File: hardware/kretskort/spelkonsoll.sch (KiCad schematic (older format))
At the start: 2 parts, among them U2 ESP32-DEVKITC-32D, U3 ILI9488

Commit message: more circuit board kicad files
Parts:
- added BZ1: Buzzer, Buzzer_Beeper:Buzzer_15x7.5RM7.6, symbol Device:Buzzer
- added SW1, SW10, SW2, SW3, SW4, SW5, SW6, SW7, SW8, SW9: SW_Push, Button_Switch_THT:SW_TH_Tactile_Omron_B3F-10xx, symbol Switch:SW_Push
- added SW11, SW12: SW_Push, Button_Switch_THT:SW_Tactile_SPST_Angled_PTS645Vx83-2LFS, symbol Switch:SW_Push
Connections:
- net +5V: now also SW1.2, SW10.2, SW11.2, SW12.2, SW2.2, SW3.2, SW4.2, SW5.2, SW6.2, SW7.2, SW8.2, SW9.2
- net GND: now also BZ1.2 (+); no longer U2.18 (CMD)
- net BTN_SELECT: now reaches U2.10 (IO26)
- net BTN_SELECT: now also SW10.1
- net BTN_DP_UP: now reaches U2.11 (IO27)
- net BTN_DP_UP: now also SW5.1
- net BTN_DP_DOWN: now reaches U2.12 (IO14)
- net BTN_DP_DOWN: now also SW6.1
- net BTN_DP_LEFT: now reaches U2.13 (IO12)
- net BTN_DP_LEFT: now also SW7.1
- net BTN_DP_RIGHT: now reaches U2.15 (IO13)
- net BTN_DP_RIGHT: now also SW8.1
- net BUZZER: now reaches U2.25 (IO21)
- net BUZZER: now also BZ1.1 (-)
- net BTN_BUMPER_L: now reaches U2.30 (IO17)
- net BTN_BUMPER_L: now also SW11.1
- net BTN_BUMPER_R: now reaches U2.31 (IO16)
- net BTN_BUMPER_R: now also SW12.1
- net BTN_A: now reaches U2.5 (IO34)
- net BTN_A: now also SW1.1
- net BTN_B: now reaches U2.6 (IO35)
- net BTN_B: now also SW2.1
- net BTN_X: now reaches U2.7 (IO32)
- net BTN_X: now also SW3.1
- net BTN_Y: now reaches U2.8 (IO33)
- net BTN_Y: now also SW4.1
- net BTN_START: now reaches U2.9 (IO25)
- net BTN_START: now also SW9.1
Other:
- note added: "BUTTONS 'N BUMPERS"
- note added: "BUZZER"
- moved on the sheet: U2, U3

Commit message: modified pcb to fit new design
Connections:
- net +5V: no longer SW1.2, SW10.2, SW11.2, SW12.2, SW2.2, SW3.2, SW4.2, SW5.2, SW6.2, SW7.2, SW8.2, SW9.2
- net GND: now also SW1.2, SW10.2, SW11.2, SW12.2, SW2.2, SW3.2, SW4.2, SW5.2, SW6.2, SW7.2, SW8.2, SW9.2
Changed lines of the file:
@@
 	1    0    0    -1
-$EndComp
-$Comp
-L power:+5V #PWR0104
-U 1 1 6203BB27
-P 9300 5100
-F 0 "#PWR0104" H 9300 4950 50  0001 C CNN
-F 1 "+5V" V 9315 5228 50  0000 L CNN
-F 2 "" H 9300 5100 50  0001 C CNN
-F 3 "" H 9300 5100 50  0001 C CNN
-	1    9300 5100
-	0    1    1    0
 $EndComp
 Wire Wire Line
@@
 Text GLabel 2850 3650 0    50   Input ~ 0
 BTN_A
-$Comp
-L power:+5V #PWR0108
-U 1 1 6203E5CA
-P 9300 5500
-F 0 "#PWR0108" H 9300 5350 50  0001 C CNN
-F 1 "+5V" V 9315 5628 50  0000 L CNN
-F 2 "" H 9300 5500 50  0001 C CNN
-F 3 "" H 9300 5500 50  0001 C CNN
-	1    9300 5500
-	0    1    1    0
-$EndComp
 Wire Wire Line
 	9200 5500 9300 5500
@@
 Text GLabel 8800 6300 0    50   Input ~ 0
 BTN_Y
-$Comp
-L power:+5V #PWR01
-U 1 1 6204640C
-P 9300 5900
-F 0 "#PWR01" H 9300 5750 50  0001 C CNN
-F 1 "+5V" V 9315 6028 50  0000 L CNN
-F 2 "" H 9300 5900 50  0001 C CNN
-F 3 "" H 9300 5900 50  0001 C CNN
-	1    9300 5900
-	0    1    1    0
-$EndComp
-$Comp
-L power:+5V #PWR02
-U 1 1 620466A0
-P 9300 6300
-F 0 "#PWR02" H 9300 6150 50  0001 C CNN
-F 1 "+5V" V 9315 6428 50  0000 L CNN
-F 2 "" H 9300 6300 50  0001 C CNN
-F 3 "" H 9300 6300 50  0001 C CNN
-	1    9300 6300
-	0    1    1    0
-$EndComp
 Wire Wire Line
 	9300 6300 9200 6300
@@
 	1    0    0    -1
 $EndComp
-$Comp
-L power:+5V #PWR0109
-U 1 1 6205AD69
-P 10800 5100
-F 0 "#PWR0109" H 10800 4950 50  0001 C CNN
-F 1 "+5V" V 10815 5228 50  0000 L CNN
-F 2 "" H 10800 5100 50  0001 C CNN
-F 3 "" H 10800 5100 50  0001 C CNN
-	1    10800 5100
-	0    1    1    0
-$EndComp
 Wire Wire Line
 	10800 5100 10700 5100
@@
 Text GLabel 10300 5500 0    50   Input ~ 0
 BTN_SELECT
-$Comp
-L power:+5V #PWR0110
-U 1 1 6205FBF8
-P 10800 5500
-F 0 "#PWR0110" H 10800 5350 50  0001 C CNN
-F 1 "+5V" V 10815 5628 50  0000 L CNN
-F 2 "" H 10800 5500 50  0001 C CNN
-F 3 "" H 10800 5500 50  0001 C CNN
-	1    10800 5500
-	0    1    1    0
-$EndComp
 Wire Wire Line
 	10800 5500 10700 5500
@@
 	1    7800 6300
 	1    0    0    -1
-$EndComp
-$Comp
-L power:+5V #PWR0111
-U 1 1 620917FA
-P 8100 5100
-F 0 "#PWR0111" H 8100 4950 50  0001 C CNN
-F 1 "+5V" V 8115 5228 50  0000 L CNN
-F 2 "" H 8100 5100 50  0001 C CNN
-F 3 "" H 8100 5100 50  0001 C CNN
-	1    8100 5100
-	0    1    1    0
-$EndComp
-$Comp
-L power:+5V #PWR0112
-U 1 1 62092742
-P 8100 5500
-F 0 "#PWR0112" H 8100 5350 50  0001 C CNN
-F 1 "+5V" V 8115 5628 50  0000 L CNN
-F 2 "" H 8100 5500 50  0001 C CNN
-F 3 "" H 8100 5500 50  0001 C CNN
-	1    8100 5500
-	0    1    1    0
-$EndComp
-$Comp
-L power:+5V #PWR0113
-U 1 1 62092987
-P 8100 5900
-F 0 "#PWR0113" H 8100 5750 50  0001 C CNN
-F 1 "+5V" V 8115 6028 50  0000 L CNN
-F 2 "" H 8100 5900 50  0001 C CNN
-F 3 "" H 8100 5900 50  0001 C CNN
-	1    8100 5900
-	0    1    1    0
-$EndComp
-$Comp
-L power:+5V #PWR0114
-U 1 1 62092C11
-P 8100 6300
-F 0 "#PWR0114" H 8100 6150 50  0001 C CNN
-F 1 "+5V" V 8115 6428 50  0000 L CNN
-F 2 "" H 8100 6300 50  0001 C CNN
-F 3 "" H 8100 6300 50  0001 C CNN
-	1    8100 6300
-	0    1    1    0
 $EndComp
 Wire Wire Line
@@
 	1    0    0    -1
 $EndComp
-$Comp
-L power:+5V #PWR0115
-U 1 1 6209A2CE
-P 10800 5900
-F 0 "#PWR0115" H 10800 5750 50  0001 C CNN
-F 1 "+5V" V 10815 6028 50  0000 L CNN
-F 2 "" H 10800 5900 50  0001 C CNN
-F 3 "" H 10800 5900 50  0001 C CNN
-	1    10800 5900
-	0    1    1    0
-$EndComp
-$Comp
-L power:+5V #PWR0116
-U 1 1 6209A652
-P 10800 6300
-F 0 "#PWR0116" H 10800 6150 50  0001 C CNN
-F 1 "+5V" V 10815 6428 50  0000 L CNN
-F 2 "" H 10800 6300 50  0001 C CNN
-F 3 "" H 10800 6300 50  0001 C CNN
-	1    10800 6300
-	0    1    1    0
-$EndComp
 Wire Wire Line
 	10800 5900 10700 5900
@@
 Text Notes 7300 4100 0    50   ~ 0
 BUZZER
+$Comp
+L power:GND #PWR?
+U 1 1 620EF8E5
+P 8100 5100
+F 0 "#PWR?" H 8100 4850 50  0001 C CNN
+F 1 "GND" V 8105 4972 50  0000 R CNN
+F 2 "" H 8100 5100 50  0001 C CNN
+F 3 "" H 8100 5100 50  0001 C CNN
+	1    8100 5100
+	0    -1   -1   0
+$EndComp
+$Comp
+L power:GND #PWR?
+U 1 1 620F3720
+P 8100 5500
+F 0 "#PWR?" H 8100 5250 50  0001 C CNN
+F 1 "GND" V 8105 5372 50  0000 R CNN
+F 2 "" H 8100 5500 50  0001 C CNN
+F 3 "" H 8100 5500 50  0001 C CNN
+	1    8100 5500
+	0    -1   -1   0
+$EndComp
+$Comp
+L power:GND #PWR?
+U 1 1 620F3932
+P 8100 5900
+F 0 "#PWR?" H 8100 5650 50  0001 C CNN
+F 1 "GND" V 8105 5772 50  0000 R CNN
+F 2 "" H 8100 5900 50  0001 C CNN
+F 3 "" H 8100 5900 50  0001 C CNN
+	1    8100 5900
+	0    -1   -1   0
+$EndComp
+$Comp
+L power:GND #PWR?
+U 1 1 620F3BCA
+P 8100 6300
+F 0 "#PWR?" H 8100 6050 50  0001 C CNN
+F 1 "GND" V 8105 6172 50  0000 R CNN
+F 2 "" H 8100 6300 50  0001 C CNN
+F 3 "" H 8100 6300 50  0001 C CNN
+	1    8100 6300
+	0    -1   -1   0
+$EndComp
+$Comp
+L power:GND #PWR?
+U 1 1 620F3D7B
+P 9300 6300
+F 0 "#PWR?" H 9300 6050 50  0001 C CNN
+F 1 "GND" V 9305 6172 50  0000 R CNN
+F 2 "" H 9300 6300 50  0001 C CNN
+F 3 "" H 9300 6300 50  0001 C CNN
+	1    9300 6300
+	0    -1   -1   0
+$EndComp
+$Comp
+L power:GND #PWR?
+U 1 1 620F4034
+P 9300 5900
+F 0 "#PWR?" H 9300 5650 50  0001 C CNN
+F 1 "GND" V 9305 5772 50  0000 R CNN
+F 2 "" H 9300 5900 50  0001 C CNN
+F 3 "" H 9300 5900 50  0001 C CNN
+	1    9300 5900
+	0    -1   -1   0
+$EndComp
+$Comp
+L power:GND #PWR?
+U 1 1 620F4234
+P 9300 5500
+F 0 "#PWR?" H 9300 5250 50  0001 C CNN
+F 1 "GND" V 9305 5372 50  0000 R CNN
+F 2 "" H 9300 5500 50  0001 C CNN
+F 3 "" H 9300 5500 50  0001 C CNN
+	1    9300 5500
+	0    -1   -1   0
+$EndComp
+$Comp
+L power:GND #PWR?
+U 1 1 620F4454
+P 9300 5100
+F 0 "#PWR?" H 9300 4850 50  0001 C CNN
+F 1 "GND" V 9305 4972 50  0000 R CNN
+F 2 "" H 9300 5100 50  0001 C CNN
+F 3 "" H 9300 5100 50  0001 C CNN
+	1    9300 5100
+	0    -1   -1   0
+$EndComp
+$Comp
+L power:GND #PWR?
+U 1 1 620F4759
+P 10800 5100
+F 0 "#PWR?" H 10800 4850 50  0001 C CNN
+F 1 "GND" V 10805 4972 50  0000 R CNN
+F 2 "" H 10800 5100 50  0001 C CNN
+F 3 "" H 10800 5100 50  0001 C CNN
+	1    10800 5100
+	0    -1   -1   0
+$EndComp
+$Comp
+L power:GND #PWR?
+U 1 1 620F4A8B
+P 10800 5500
+F 0 "#PWR?" H 10800 5250 50  0001 C CNN
+F 1 "GND" V 10805 5372 50  0000 R CNN
+F 2 "" H 10800 5500 50  0001 C CNN
+F 3 "" H 10800 5500 50  0001 C CNN
+	1    10800 5500
+	0    -1   -1   0
+$EndComp
+$Comp
+L power:GND #PWR?
+U 1 1 620F4CC5
+P 10800 5900
+F 0 "#PWR?" H 10800 5650 50  0001 C CNN
+F 1 "GND" V 10805 5772 50  0000 R CNN
+F 2 "" H 10800 5900 50  0001 C CNN
+F 3 "" H 10800 5900 50  0001 C CNN
+	1    10800 5900
+	0    -1   -1   0
+$EndComp
+$Comp
+L power:GND #PWR?
+U 1 1 620F4F07
+P 10800 6300
+F 0 "#PWR?" H 10800 6050 50  0001 C CNN
+F 1 "GND" V 10805 6172 50  0000 R CNN
+F 2 "" H 10800 6300 50  0001 C CNN
+F 3 "" H 10800 6300 50  0001 C CNN
+	1    10800 6300
+	0    -1   -1   0
+$EndComp
 $EndSCHEMATC

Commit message: added power circuit
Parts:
- added BT1: Battery_Cell, Battery:BatteryHolder_MPD_BH-18650-PC2, symbol Device:Battery_Cell
- added C1, C2: C_Small, symbol Device:C_Small
- added D1: LED, symbol Device:LED
- added J1: USB_C_Receptacle_USB2.0, Connector_USB:USB_C_Receptacle_Amphenol_12401610E4-2A, symbol Connector:USB_C_Receptacle_USB2.0
- added R1: 330, symbol Device:R
- added R2: R, symbol Device:R
- added U1: BQ24202DGN, Strøm:BQ24202DGN, symbol Strøm:BQ24202DGN
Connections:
- net +5V: now also U3.8 (LED)
- net GND: now also C1.1, C2.2, J1.A1 (GND), J1.A12 (GND), J1.B1 (GND), J1.B12 (GND), R1.2, R2.2, U1.4 (VSS), U1.9 (EPAD)
- new net: D1.2 (A), U1.3 (STAT)
- new net: BT1.2 (-), R2.1, U1.6 (~CE)
- new net: BT1.1 (+), C2.1, U1.7 (BAT), U1.8 (OUT)
- new net: D1.1 (K), R1.1
- new net USB_PWR: C1.2, J1.A4 (VBUS), J1.A9 (VBUS), J1.B4 (VBUS), J1.B9 (VBUS), U1.1 (IN), U1.2 (VCC)
- no-connect marks 9 -> 17
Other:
- note added: "Sjekk om dette er no no å gjøre"

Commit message: lol glemte å lagre
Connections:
- no-connect marks 17 -> 34
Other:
- moved on the sheet: BT1, C1, C2, D1, J1, R1, R2, U1

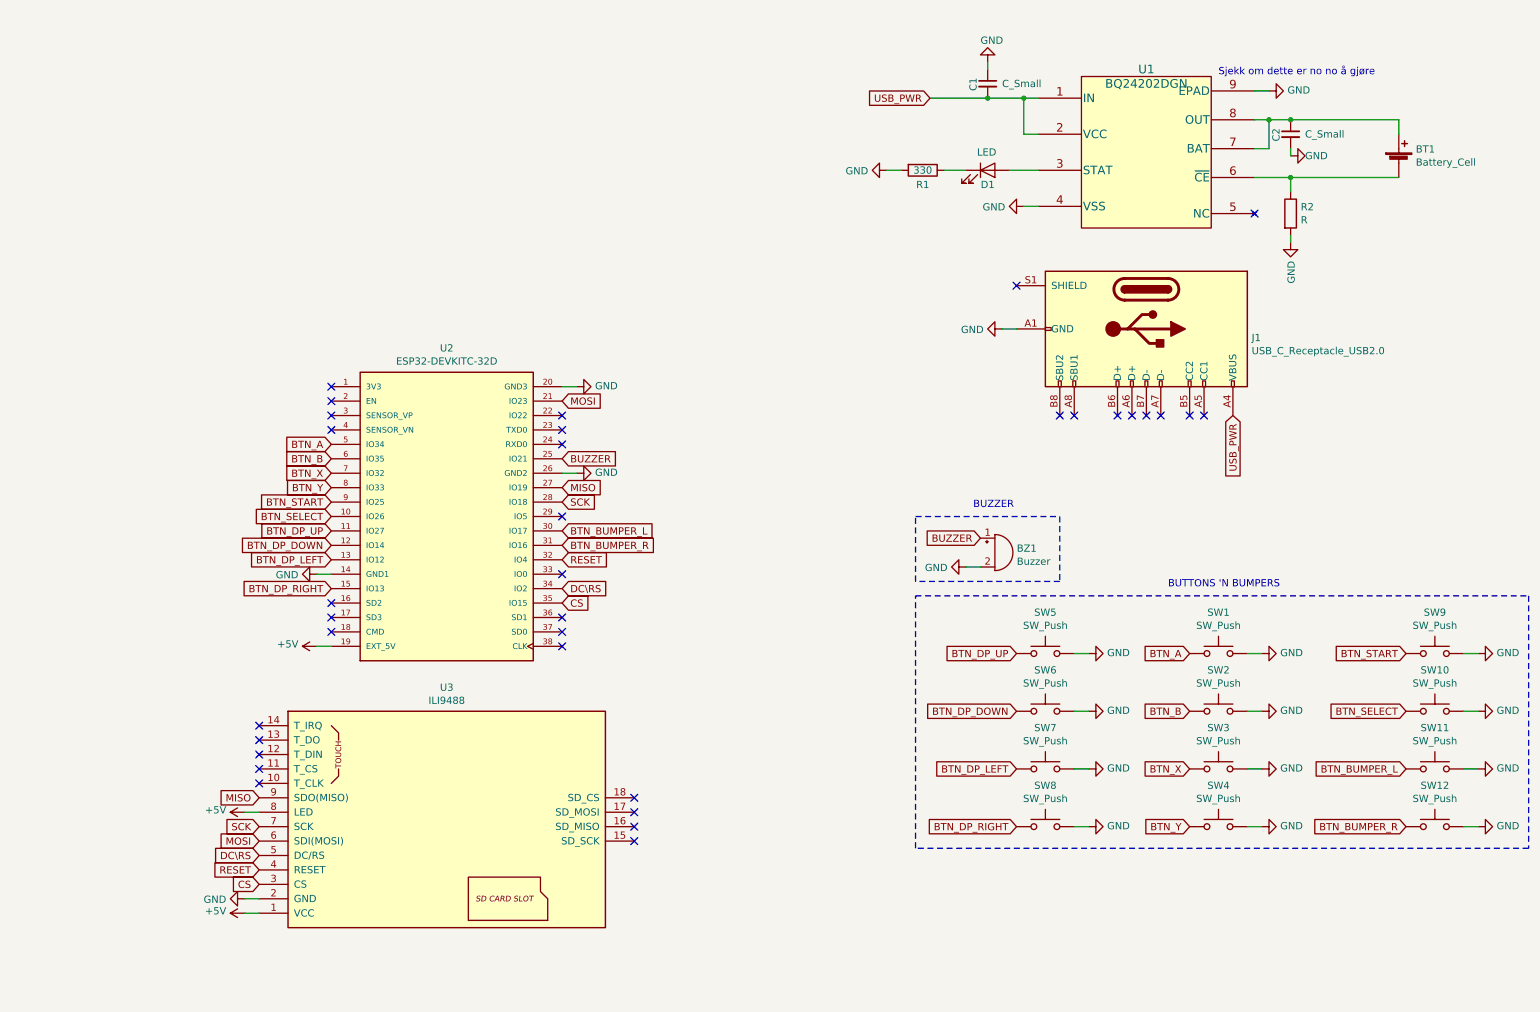
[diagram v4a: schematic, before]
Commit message: modified buttons to maybe work
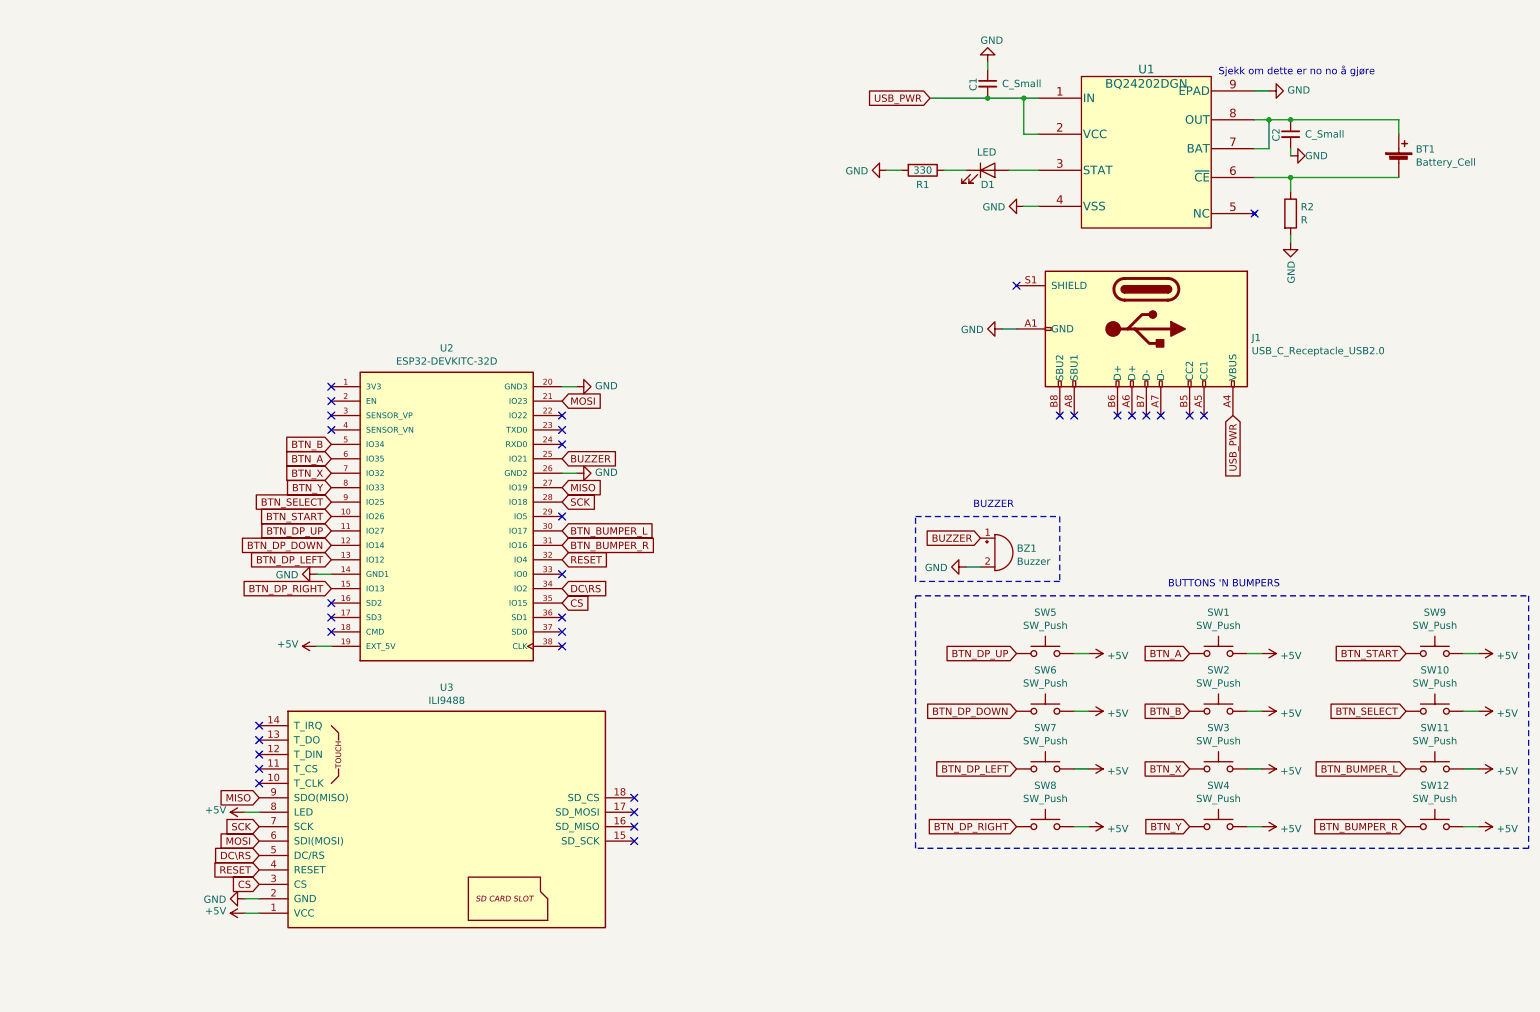
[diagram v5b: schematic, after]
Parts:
- BT1: footprint Battery:BatteryHolder_MPD_BH-18650-PC2 -> footprints:18650holder
- J1: footprint Connector_USB:USB_C_Receptacle_Amphenol_12401610E4-2A -> (none)
- SW1, SW10, SW2, SW3, SW4, SW5, SW6, SW7, SW8, SW9: footprint Button_Switch_THT:SW_TH_Tactile_Omron_B3F-10xx -> footprints:B3F1052
- SW11, SW12: footprint Button_Switch_THT:SW_Tactile_SPST_Angled_PTS645Vx83-2LFS -> footprints:B3F-3152
- U1: footprint Strøm:BQ24202DGN -> (none)
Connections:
- net +5V: now also SW1.2, SW10.2, SW11.2, SW12.2, SW2.2, SW3.2, SW4.2, SW5.2, SW6.2, SW7.2, SW8.2, SW9.2
- net BTN_A: now also U2.6 (IO35); no longer U2.5 (IO34)
- net BTN_B: now also U2.5 (IO34); no longer U2.6 (IO35)
- net BTN_SELECT: now also U2.9 (IO25); no longer U2.10 (IO26)
- net BTN_START: now also U2.10 (IO26); no longer U2.9 (IO25)
- net GND: no longer SW1.2, SW10.2, SW11.2, SW12.2, SW2.2, SW3.2, SW4.2, SW5.2, SW6.2, SW7.2, SW8.2, SW9.2

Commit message: added modified files for new circuit
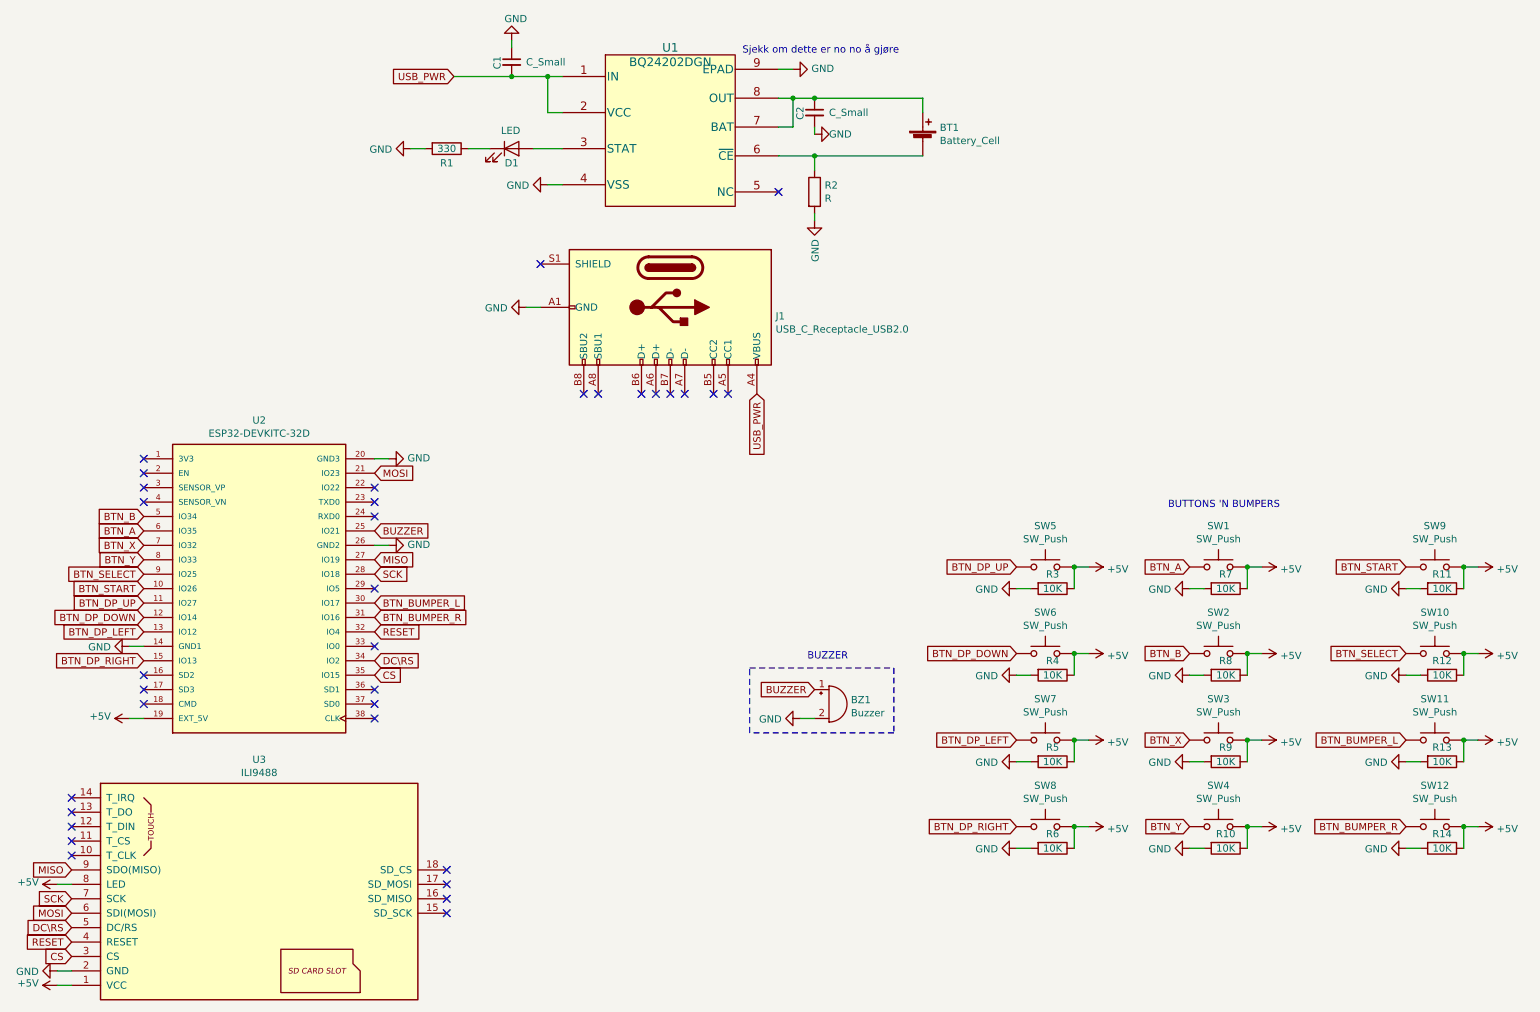
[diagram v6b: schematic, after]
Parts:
- added R10, R11, R12, R13, R14, R3, R4, R5, R6, R7, R8, R9: 10K, Resistor_THT:R_Axial_DIN0207_L6.3mm_D2.5mm_P7.62mm_Horizontal, symbol Device:R
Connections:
- net +5V: now also R10.1, R11.1, R12.1, R13.1, R14.1, R3.1, R4.1, R5.1, R6.1, R7.1, R8.1, R9.1
- net GND: now also R10.2, R11.2, R12.2, R13.2, R14.2, R3.2, R4.2, R5.2, R6.2, R7.2, R8.2, R9.2
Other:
- moved on the sheet: BT1, BZ1, C1, C2, D1, J1, R1, R2, SW1, SW10, SW11, SW2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
